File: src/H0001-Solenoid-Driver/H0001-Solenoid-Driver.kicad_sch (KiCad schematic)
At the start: 12 parts

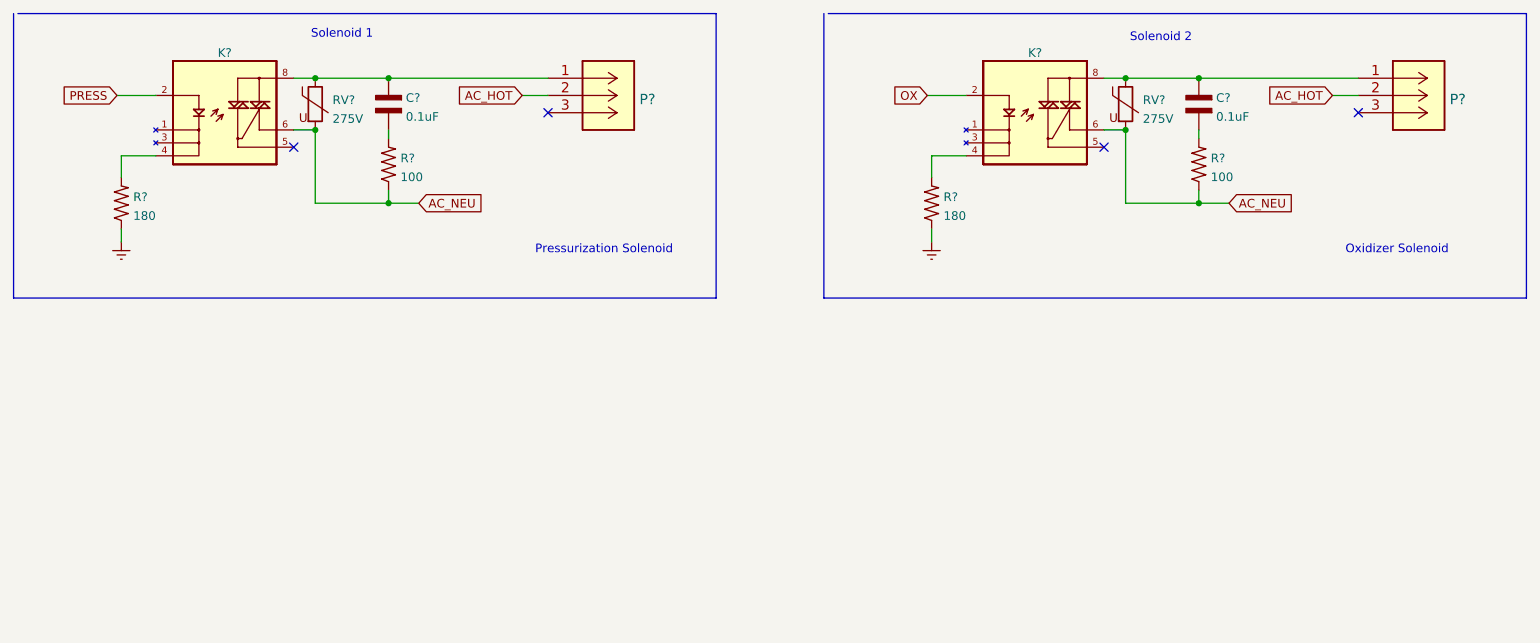
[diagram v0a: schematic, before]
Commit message: Added connectors to schematic
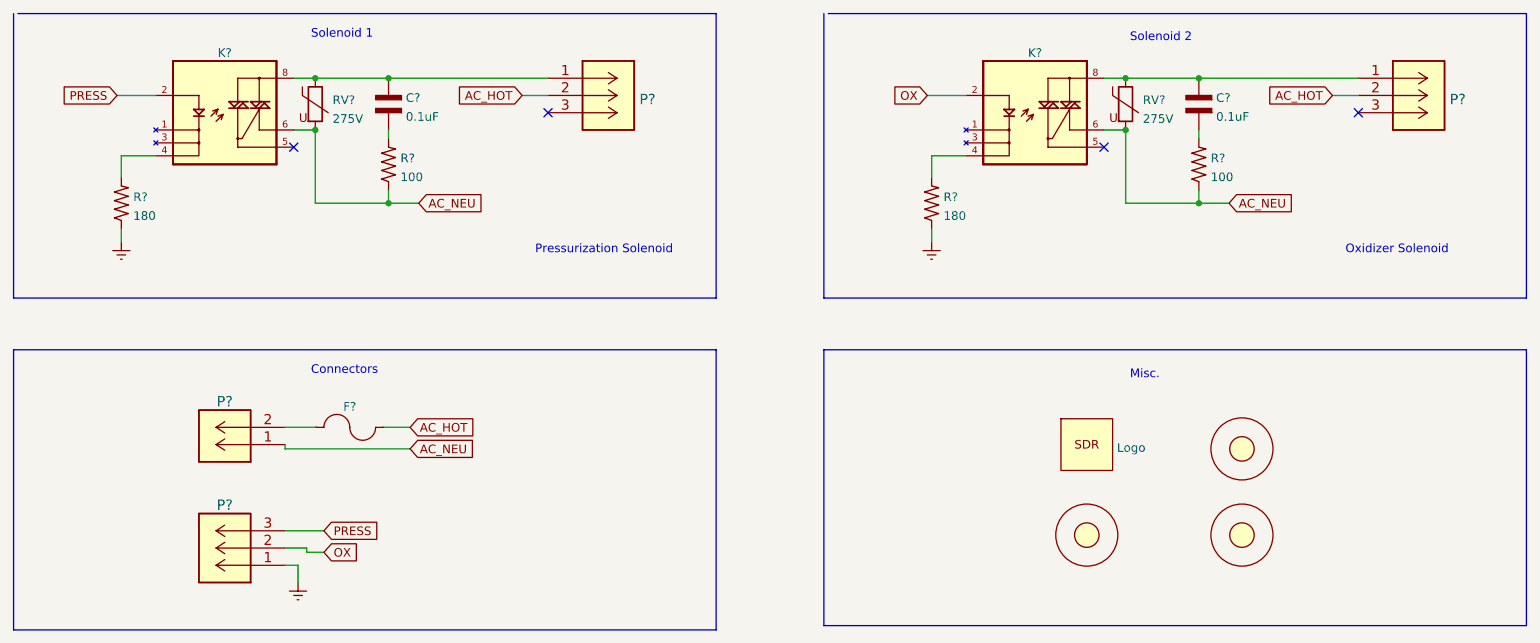
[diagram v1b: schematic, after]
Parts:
- added F?: 0678L9100-02, FUSC9830X318N, symbol H0001-Solenoid-Driver:0678L9100-02
- added H? (x3): Mounting-Hole, symbol H0001-Solenoid-Driver:Mounting-Hole
- added LOGO?: Logo, symbol H0001-Solenoid-Driver:Logo
- added P?: 647676-2, CONN_2043-1X04G00DAU_OUP, symbol H0001-Solenoid-Driver:647676-2
- added P?: 647676-3, CONN_2043-1X04G00DAU_OUP, symbol H0001-Solenoid-Driver:647676-3
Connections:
- net AC_HOT: now also F?.2
- net AC_NEU: now also P?.1
- net Earth: now also P?.1
- net OX: now also P?.2
- net PRESS: now also P?.3
- new net: F?.1, P?.2
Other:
- note added: "Connectors"
- note added: "Misc."
